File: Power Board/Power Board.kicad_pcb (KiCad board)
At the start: 2 copper layers, 55.9 x 58.4 mm, 151 parts, among them J1 Conn_02x03_Odd_Even, J2 Conn_01x02, J3 Conn_01x02, J4 Conn_01x02, J5 Conn_01x02, J6 Conn_01x02, J7 Conn_01x03, J8 Conn_02x07_Odd_Even, Q1 SI7157DP, Q2 SI7157DP, Q3 SI7157DP, Q4 SI7157DP, Q5 SI7157DP, Q6 SI7157DP, Q7 DMG2305UX, U1 LTC4417CGN, U10 LMR62014XMF, U11 TPS22810, U2 TPS564208DDCT, U3 LTC3130-1, U4 BQ2057WSNTR, U5 BQ29209DRBT, U6 LT6700CS6-1, U7 STS8C5H30L, U8 LTC4150, U9 ATxmega32E5-AU

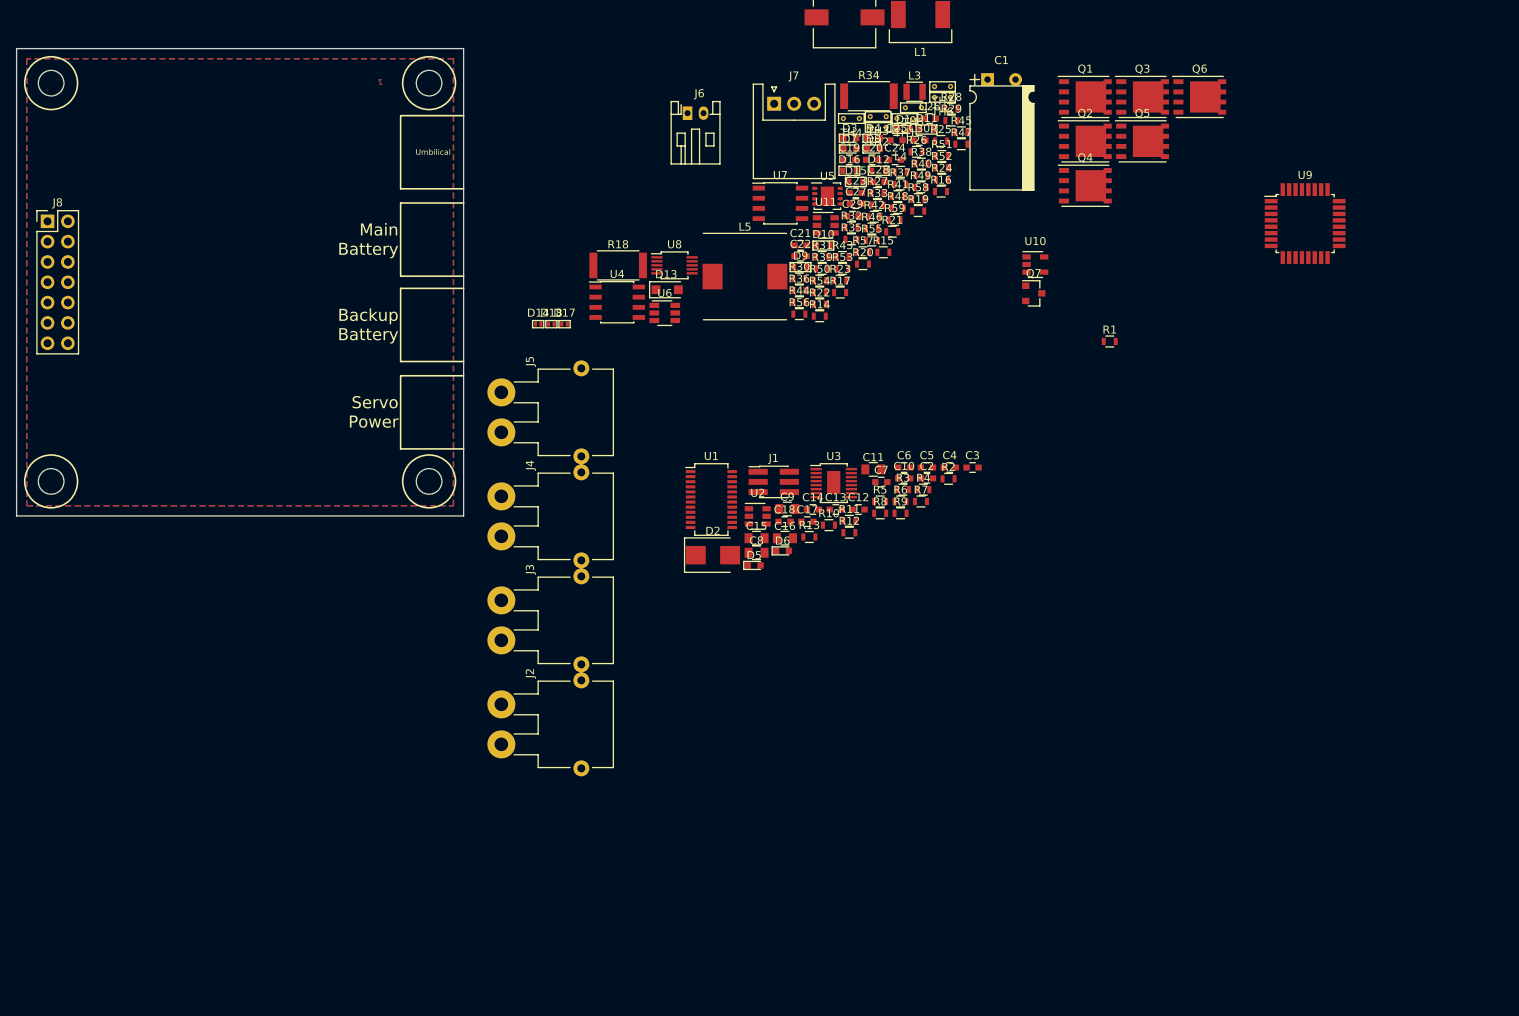
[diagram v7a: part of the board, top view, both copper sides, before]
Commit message: Made board bigger, started layout
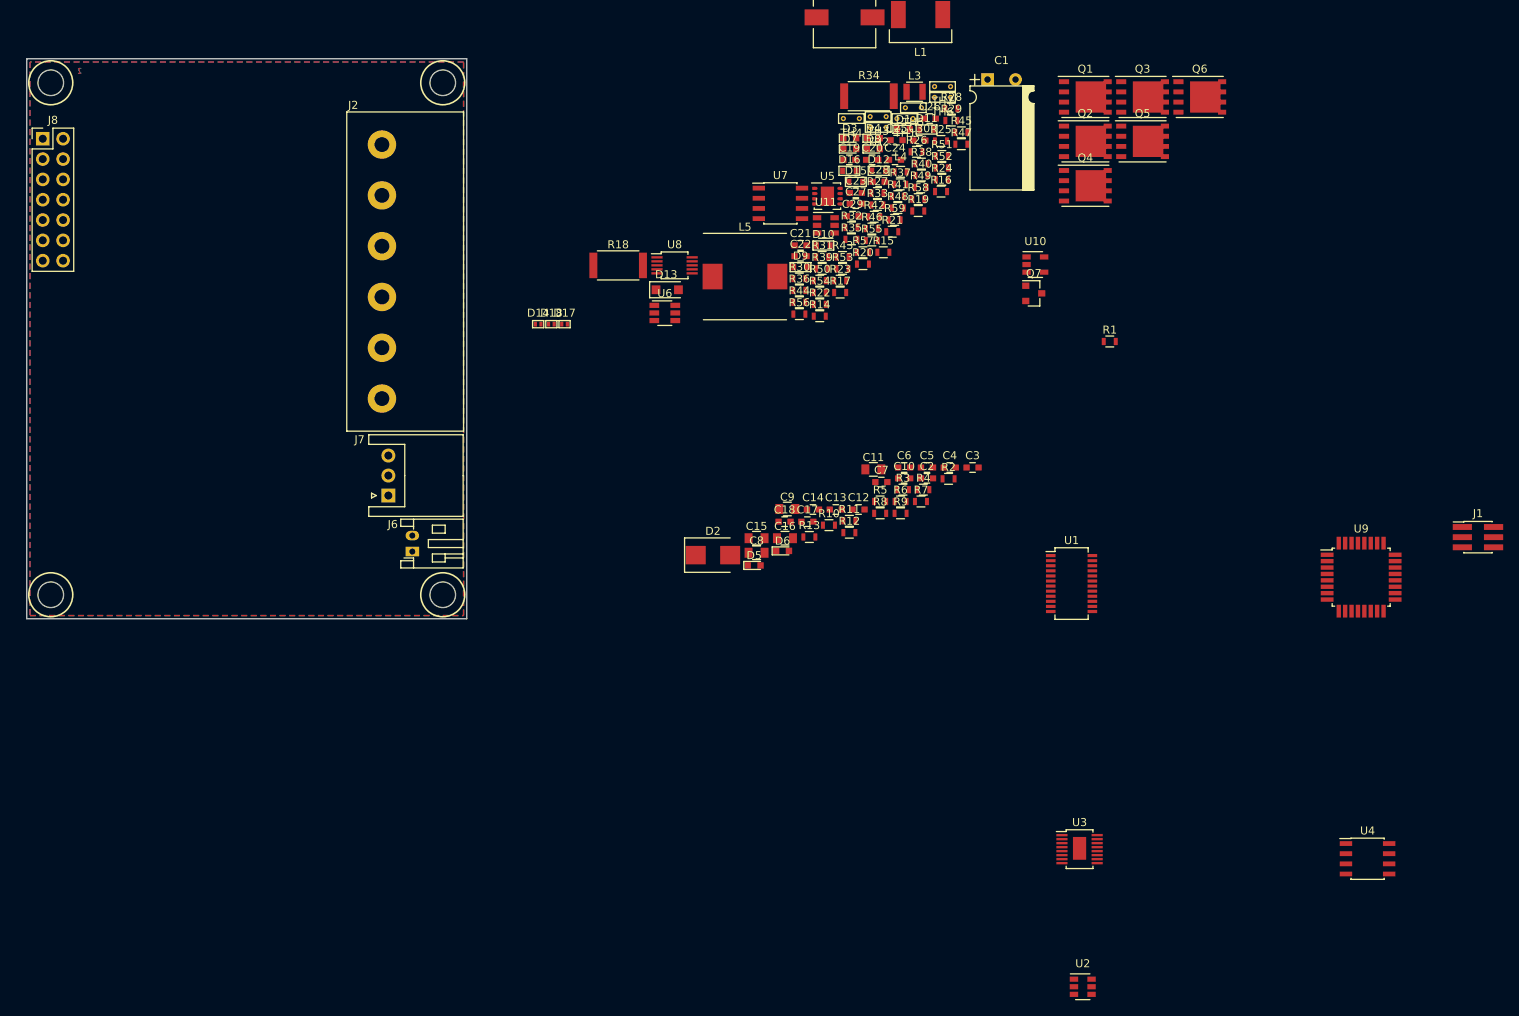
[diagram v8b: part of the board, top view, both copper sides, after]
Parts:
- removed J3, J4, J5: Conn_01x02, Custom Parts:XT30_Angled
- J2: value Conn_01x02 -> Screw_Terminal_01x06; footprint Custom Parts:XT30_Angled -> Custom Parts:3PCV-06
- moved U4 116.8 mm to (364.7, 184.3)
- moved J1 88.3 mm to (378.5, 144.1)
- moved HS1 85.4 mm to (347.9, 61.1)
- moved U2 71.5 mm to (329.1, 200.3)
- moved J7 68.7 mm to (242.3, 138.9), turned to 90 degrees
- moved J6 64.7 mm to (245.3, 145.9), turned to 90 degrees
- moved J2 58.5 mm to (241.5, 110.9), turned to 90 degrees
- moved U3 55.1 mm to (328.7, 183.1)
- moved U1 46.2 mm to (327.7, 149.9)
- moved U9 44.8 mm to (363.9, 149.1)
- moved H4 14.3 mm to (249.1, 151.3)
- moved H3 14.2 mm to (200.1, 151.3)
- moved J8 10.3 mm to (199.1, 94.3)
- moved H2 1.71 mm to (249.1, 87.3)
- moved H1 0.07 mm to (200.1, 87.3)
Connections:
- J2 pad 1: /VCC_IN -> /BAT_CELL_2_CONN
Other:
- board size 55.9 x 58.4 mm -> 55 x 70 mm
- board text removed: "Backup Battery"
- board text removed: "Main Battery"
- board text removed: "Servo Power"
- board text removed: "Umbilical"
